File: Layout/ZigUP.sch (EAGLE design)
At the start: 36 parts, among them IC1 IRM-02-3.3, IC2 CC2530, K1 DSP2A-L2-DC3V, T1 IRFML8244, T2 IRFML8244, X1 Phoenix 1792876, X2 TE 1-2834021-4, X3 TE 1-2834021-4, X4 DEBUG

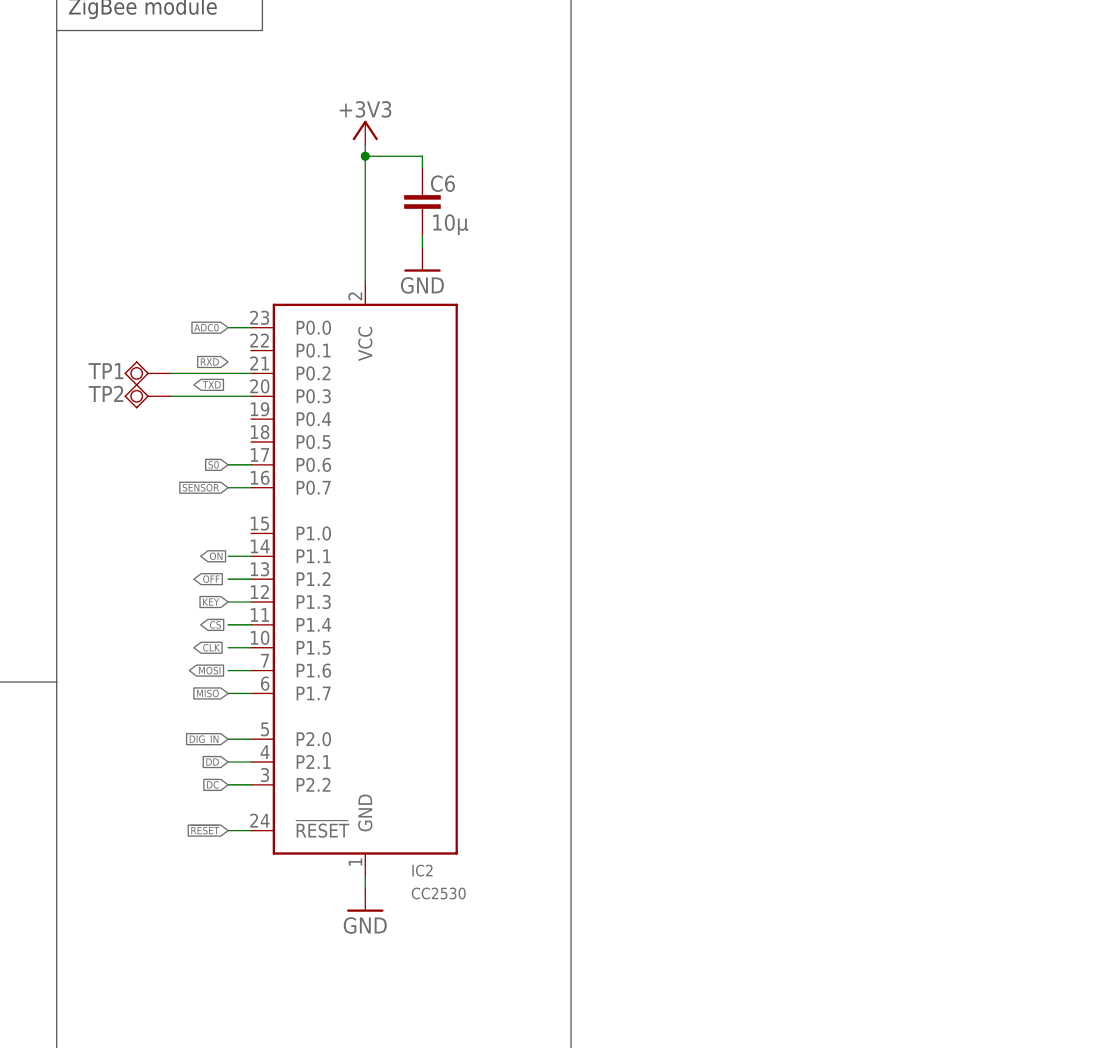
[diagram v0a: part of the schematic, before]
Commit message: Added accelerometer MMA845x
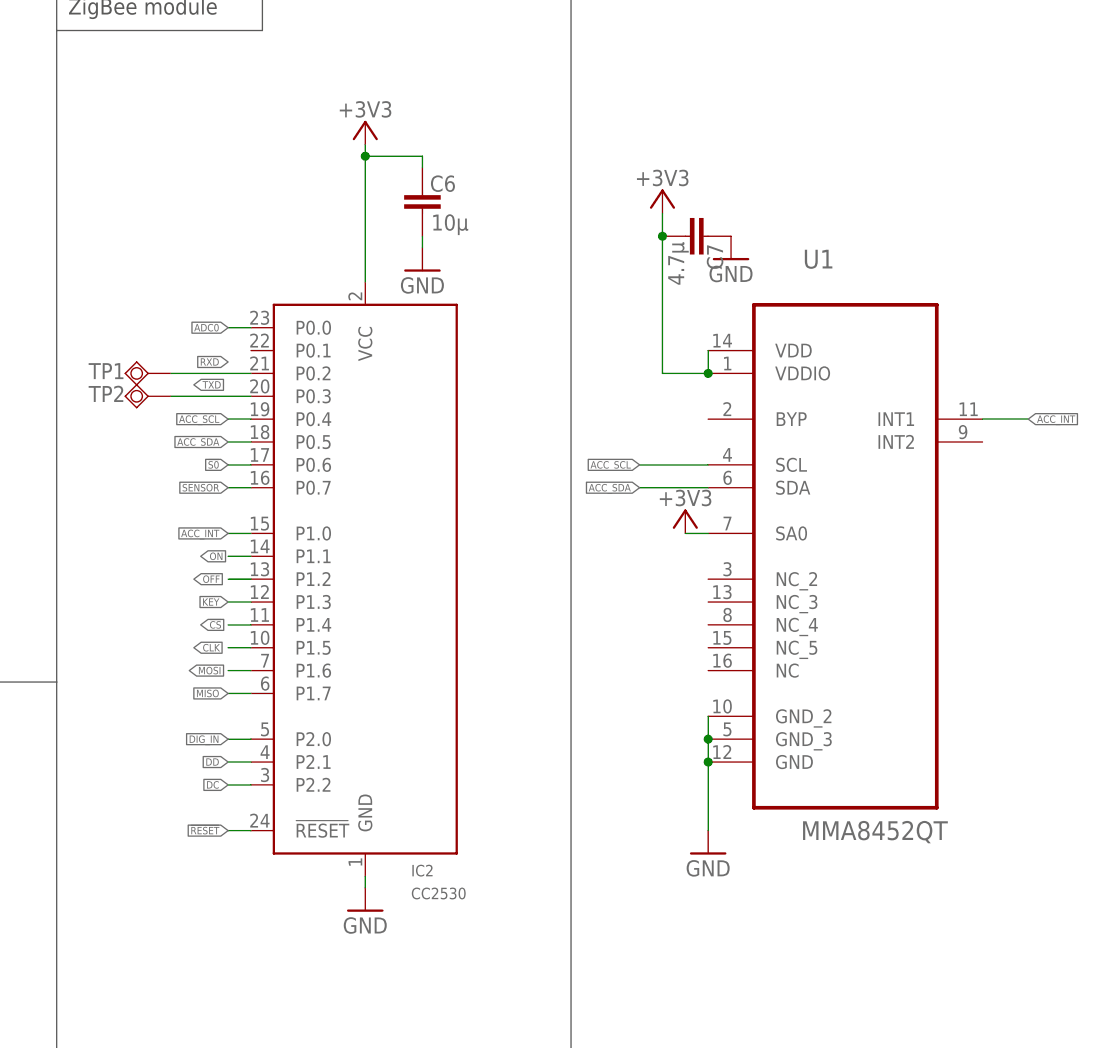
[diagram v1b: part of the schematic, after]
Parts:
- added C7: 4.7µ, rcl:C-EUC0805
- added U1: MMA8452QT, mma8452:MMA8452QT
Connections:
- new net ACC_INT: IC2.P1.0, U1.INT1
- new net ACC_SCL: IC2.P0.4, U1.SCL
- new net ACC_SDA: IC2.P0.5, U1.SDA
- net +3V3: now also C7.2, U1.SA0, U1.VDD, U1.VDDIO
- net GND: now also C7.1, U1.GND, U1.GND_2, U1.GND_3

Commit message: final release version
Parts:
- added C8, C9: 100n, rcl:C-EUC0805
- added LED1: RED, led:LED3MM
- added LED2: (no value), led:LEDSML0805
- added R11, R12, R13: 10k, rcl:R-EU_R0805
- added R14: (no value), rcl:R-EU_R0805
- C2: device rcl:CPOL-EUD -> rcl:CPOL-EUE2.5-6
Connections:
- new net LED: IC2.P0.1, R13.2
- new net N$1: C9.2, U1.BYP
- new net N$2: LED1.A, R13.1
- new net N$9: LED2.A, R14.2
- net +3V3: now also C8.2, R11.2, R12.2, R14.1
- net ACC_SCL: now also R11.1
- net ACC_SDA: now also R12.1
- net GND: now also C8.1, C9.1, LED1.C, LED2.C
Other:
- note added: "Accelerometer"
- moved on the sheet: C7, U1
